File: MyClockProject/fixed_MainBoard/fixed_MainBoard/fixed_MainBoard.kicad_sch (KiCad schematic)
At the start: 23 parts, among them J1 Conn_01x16_Socket_ESP32, J2 Conn_01x16_Socket_ESP32, J3 USB_C_Receptacle_PowerOnly_6P, J4 RJ45, J5 Conn_01x05_Socket, J6 Conn_01x05_Pin, J7 Barrel_Jack, J8 Conn_01x03_Socket, J9 Conn_01x03_Pin, U1 ULN2003A, U2 HallSensor A3144, U3 SH-U12

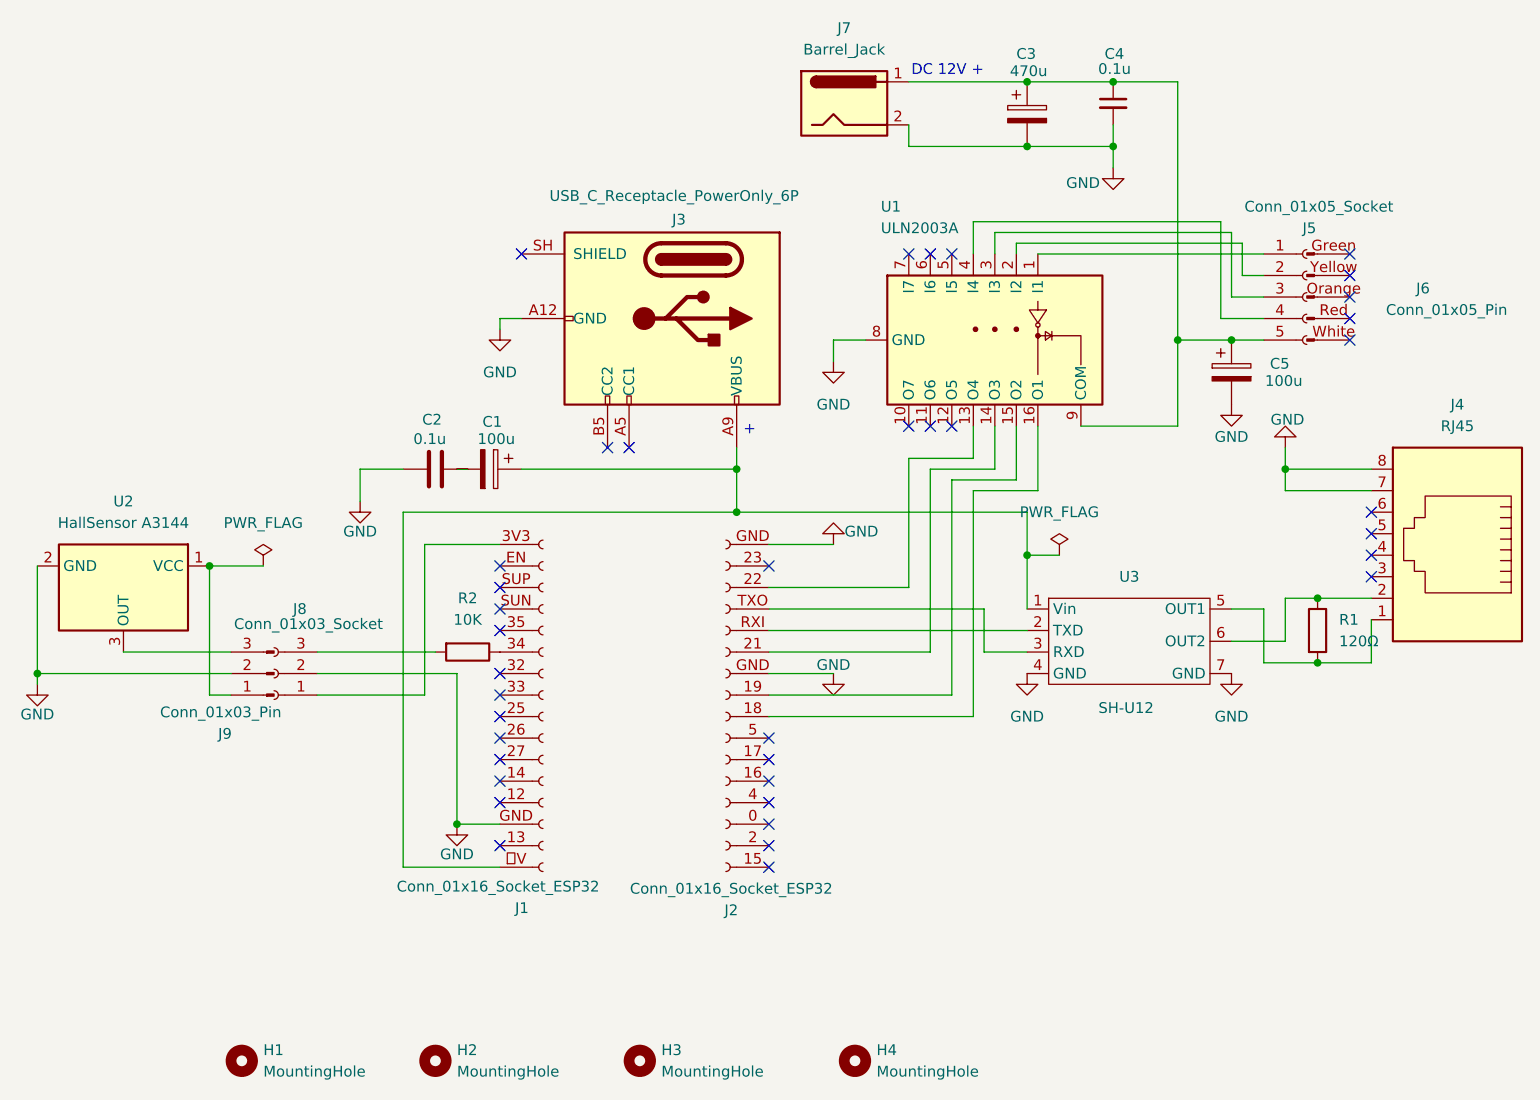
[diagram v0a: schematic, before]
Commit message: main_Boardのschファイル（回路図）のセンサーコネクト部分にプルアップ抵抗を追加しました。pcbファイルが破損していたので、書き直しています（未完成）。SwitchBoxの参照をしましたが、変更はしていません。
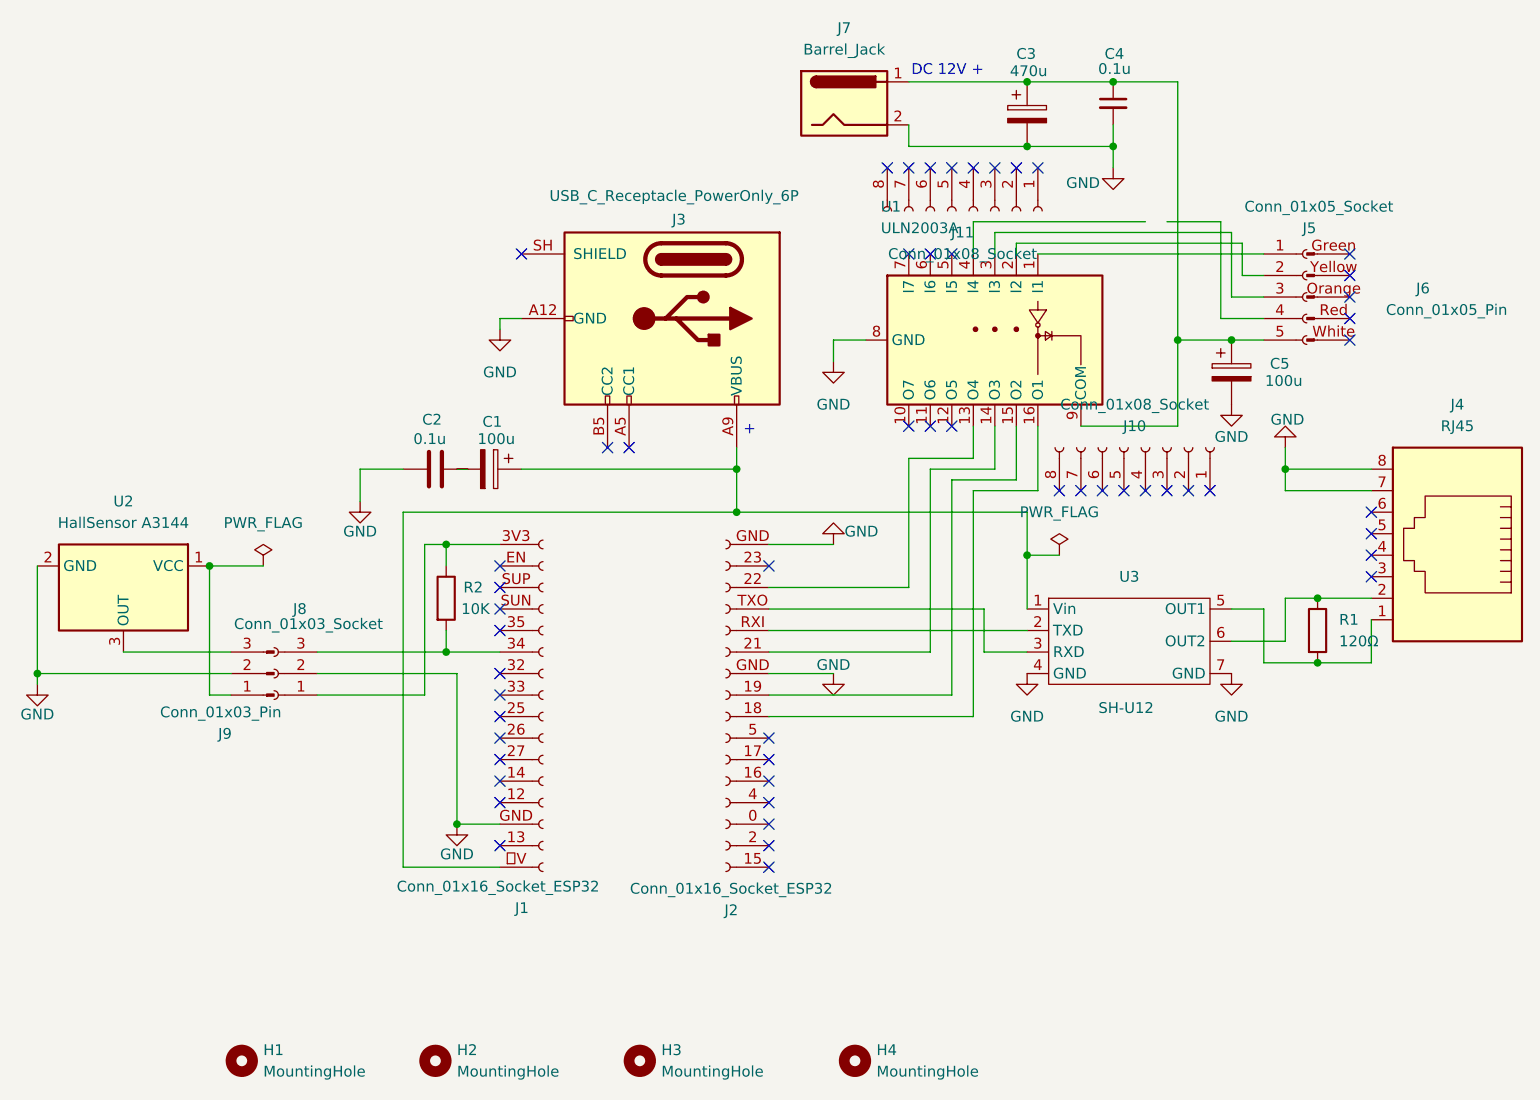
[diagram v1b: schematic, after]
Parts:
- added J10, J11: Conn_01x08_Socket, Connector_PinSocket_2.54mm:PinSocket_1x08_P2.54mm_Vertical, symbol Connector:Conn_01x08_Socket
- J3: footprint (none) -> Connector_USB:USB_C_Receptacle_GCT_USB4125-xx-x-0190_6P_TopMnt_Horizontal
- J4: footprint Connector_RJ:RJ45_RCH_RC01937 -> Connector_RJ:RJ12_Amphenol_54601-x06_Horizontal
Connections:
- net at U1.4 (I4): no longer J5.4 (Pin_4)
- net at J1.34 (Pin_6): now also J8.3 (Pin_3), R2.2; no longer R2.1
- net at J1.3V3 (Pin_1), J8.1 (Pin_1): now also R2.1
- no-connect marks 38 -> 54
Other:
- moved on the sheet: R2
